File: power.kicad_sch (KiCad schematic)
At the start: 32 parts, among them J1 Barrel_Jack_MountingPin, J3 Conn_02x04_Odd_Even, Q1 SI2301CDS-T1-GE3, SW1 Power, U1 TPS54302

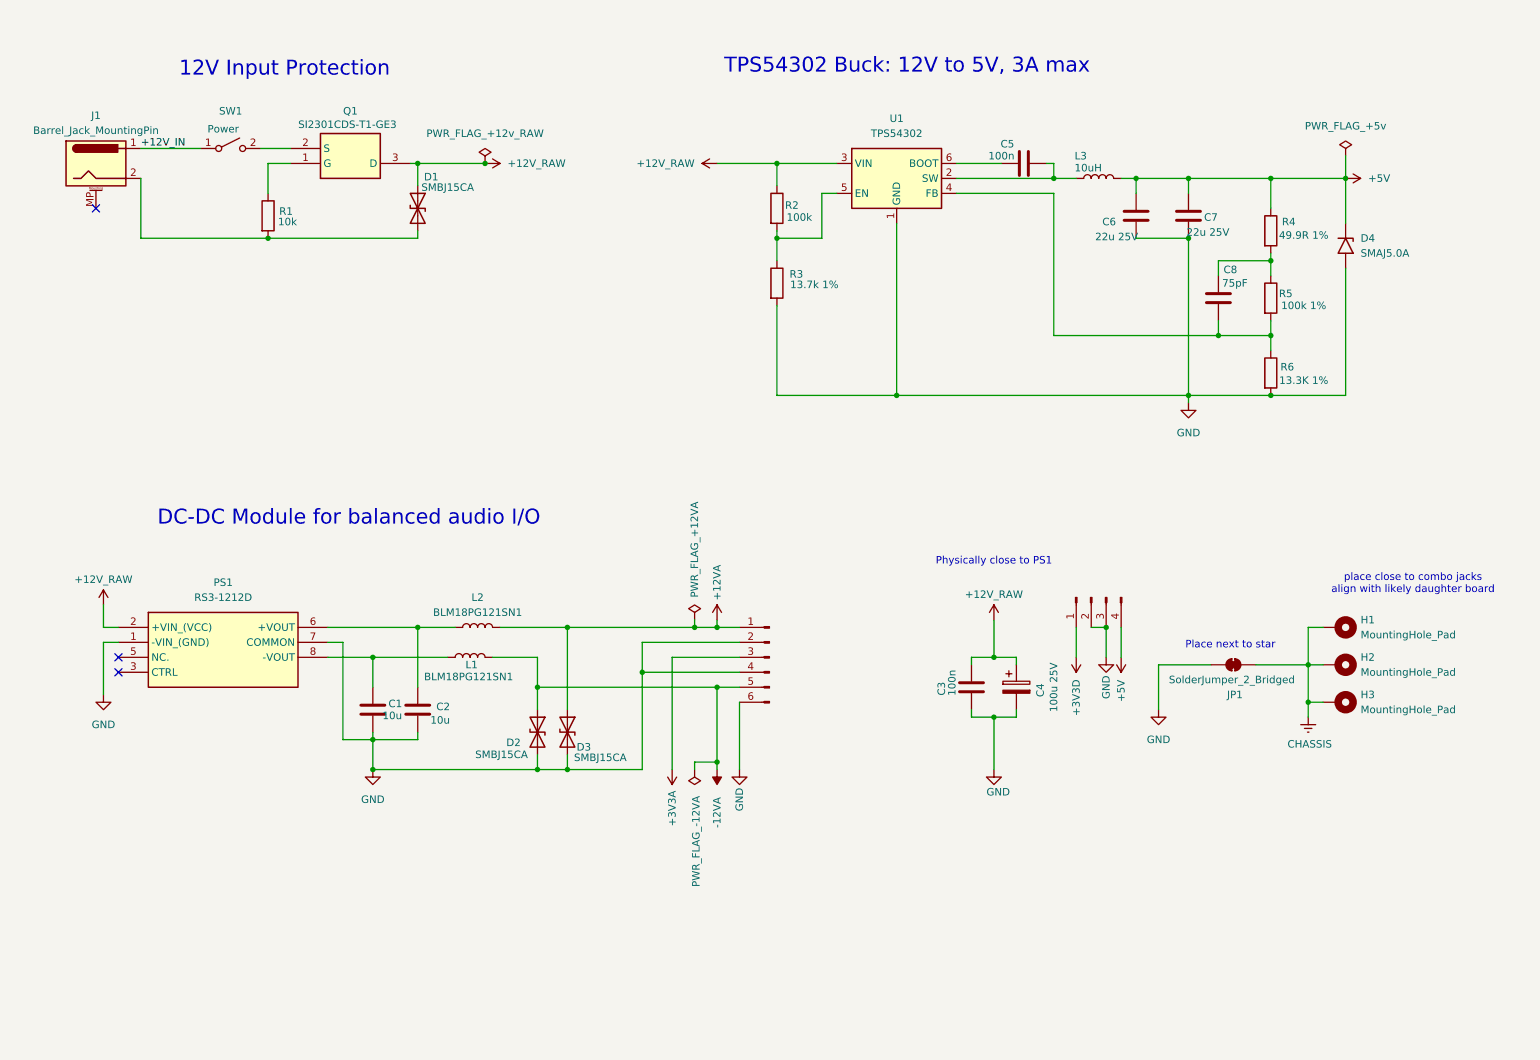
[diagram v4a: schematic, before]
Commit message: clean up some power cap issues
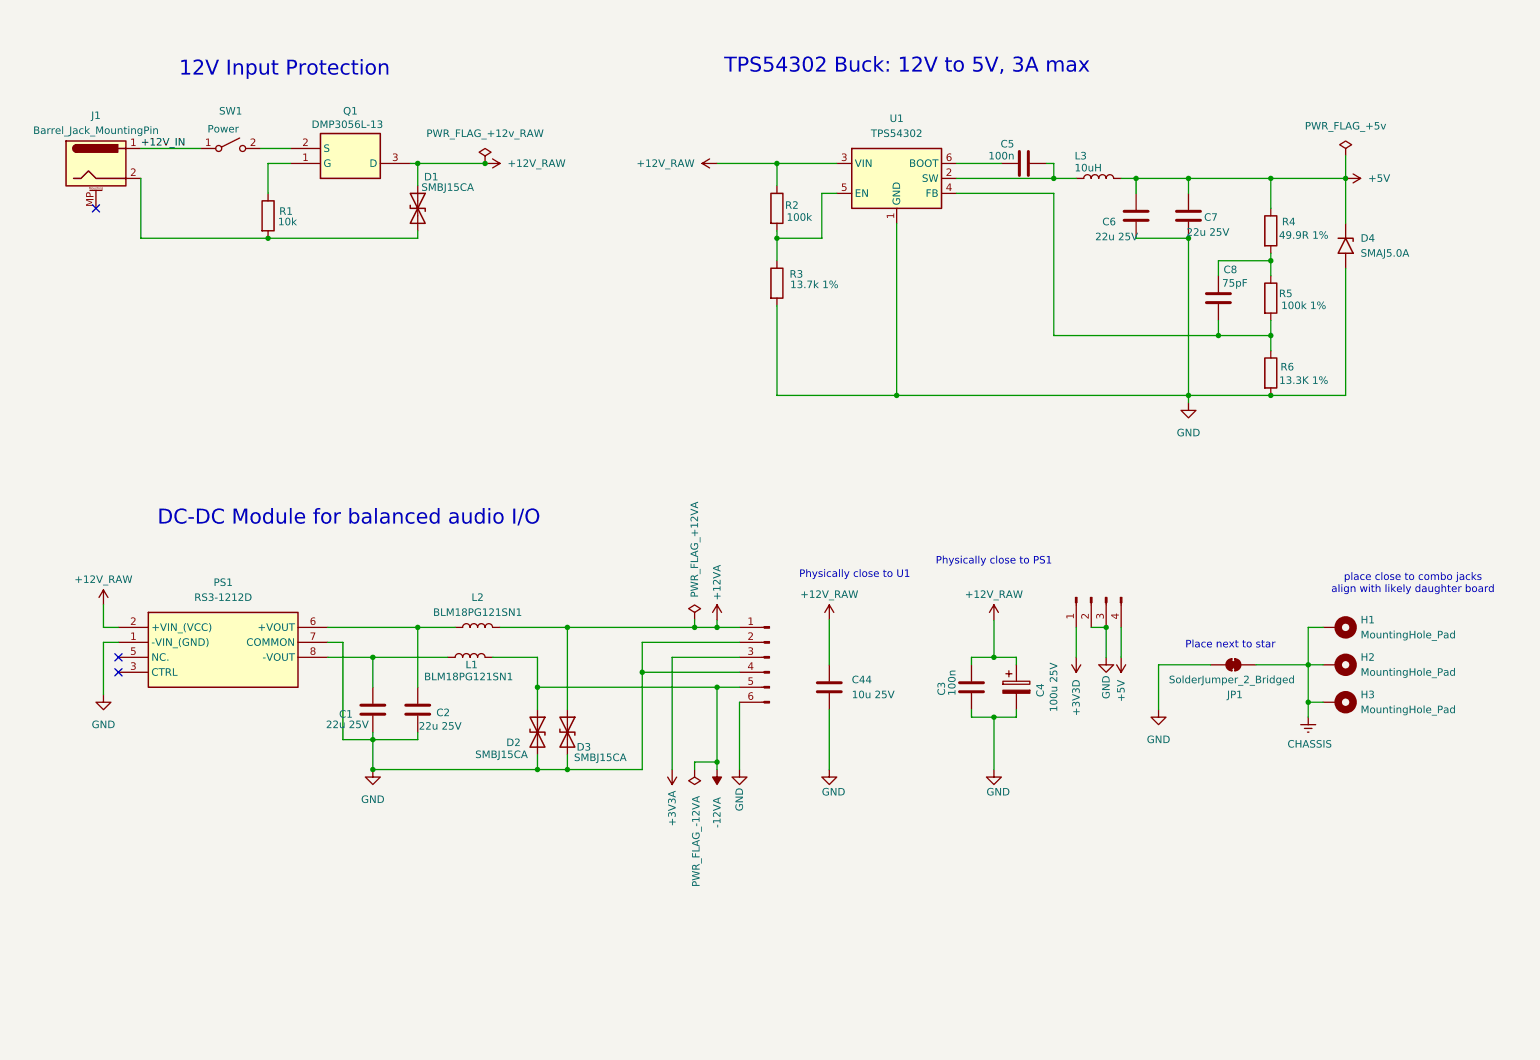
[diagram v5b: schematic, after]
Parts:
- added C44: 10u 25V, Capacitor_SMD:C_1206_3216Metric, symbol Device:C
- C1, C2: value 10u -> 22u 25V; footprint Capacitor_SMD:C_0805_2012Metric -> Capacitor_SMD:C_1206_3216Metric
- J3: value Conn_02x04_Odd_Even -> Conn_02x02_Odd_Even; footprint Connector_PinHeader_2.54mm:PinHeader_2x04_P2.54mm_Vertical -> Connector_PinHeader_2.54mm:PinHeader_2x02_P2.54mm_Vertical
- Q1: value SI2301CDS-T1-GE3 -> DMP3056L-13; footprint daisy-studio:SOT95P237X112-3N -> Package_TO_SOT_SMD:SOT-23-3; Manufacturer_Name Vishay -> Diodes Incorporated; Manufacturer_Part_Number SI2301CDS-T1-GE3 -> DMP3056L-13; Mouser Part Number 781-SI2301CDS-T1-GE3 -> 621-DMP3056L-13; Mouser Price/Stock https://www.mouser.co.uk/ProductDetail/Vishay-Semiconductor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 -> https://www.mouser.com/ProductDetail/Diodes-Incorporated/DM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
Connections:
- net +12V_RAW: now also C44.1
- net GND: now also C44.2
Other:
- note added: "Physically close to U1"

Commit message: final layout
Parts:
- renumbered C4 to C36, C5 to C37, C8 to C38, C44 to C39, C6 to C40, C7 to C41, C3 to C42, C2 to C43, C1 to C44, D3 to D12, D2 to D13, D1 to D14, D4 to D15, H2 to H4, H3 to H7, J3 to J12, J1 to J13, J2 to J8, L3 to L1, L1 to L3, Q1 to Q5, R1 to R33, R2 to R34, R5 to R35, R4 to R36, R3 to R37, R6 to R38, U1 to U10
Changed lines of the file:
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@@
 		(on_board yes)
 		(dnp no)
-		(property "Reference" "J2"
+		(property "Reference" "J8"
 			(at 139.192 141.224 90)
 			(effects
@@
 			(project "daisy-studio"
 				(path "/55cca6a8-30da-4c13-b2f2-a01401e2b54c/a1b2c3d4-1111-4000-8000-000000000001"
-					(reference "J2")
+					(reference "J8")
 					(unit 1)
 				)
@@
 		(on_board yes)
 		(dnp no)
-		(property "Reference" "C8"
+		(property "Reference" "C38"
 			(at 217.932 67.564 0)
 			(effects
@@
 			(project "triptech"
 				(path "/55cca6a8-30da-4c13-b2f2-a01401e2b54c/a1b2c3d4-1111-4000-8000-000000000001"
-					(reference "C8")
+					(reference "C38")
 					(unit 1)
 				)
@@
 		(on_board yes)
 		(dnp no)
-		(property "Reference" "J3"
+		(property "Reference" "J12"
 			(at 202.184 123.698 90)
 			(effects
@@
 			(project "daisy-studio"
 				(path "/55cca6a8-30da-4c13-b2f2-a01401e2b54c/a1b2c3d4-1111-4000-8000-000000000001"
-					(reference "J3")
+					(reference "J12")
 					(unit 1)
 				)
@@
 		(on_board yes)
 		(dnp no)
-		(property "Reference" "C1"
+		(property "Reference" "C44"
 			(at 67.818 143.002 0)
 			(effects
@@
 			(project "triptech"
 				(path "/55cca6a8-30da-4c13-b2f2-a01401e2b54c/a1b2c3d4-1111-4000-8000-000000000001"
-					(reference "C1")
+					(reference "C44")
 					(unit 1)
 				)
@@
 		(dnp no)
 		(fields_autoplaced yes)
-		(property "Reference" "C44"
+		(property "Reference" "C39"
 			(at 153.67 137.1599 0)
 			(effects
@@
 			(project ""
 				(path "/55cca6a8-30da-4c13-b2f2-a01401e2b54c/a1b2c3d4-1111-4000-8000-000000000001"
-					(reference "C44")
+					(reference "C39")
 					(unit 1)
 				)
@@
 		(on_board yes)
 		(dnp no)
-		(property "Reference" "R4"
+		(property "Reference" "R36"
 			(at 227.838 59.436 0)
 			(effects
@@
 			(project "triptech"
 				(path "/55cca6a8-30da-4c13-b2f2-a01401e2b54c/a1b2c3d4-1111-4000-8000-000000000001"
-					(reference "R4")
+					(reference "R36")
 					(unit 1)
 				)
@@
 		(on_board yes)
 		(dnp no)
-		(property "Reference" "C7"
+		(property "Reference" "C41"
 			(at 214.63 58.674 0)
 			(effects
@@
 			(project "triptech"
 				(path "/55cca6a8-30da-4c13-b2f2-a01401e2b54c/a1b2c3d4-1111-4000-8000-000000000001"
-					(reference "C7")
+					(reference "C41")
 					(unit 1)
 				)
@@
 		(on_board yes)
 		(dnp no)
-		(property "Reference" "D3"
+		(property "Reference" "D12"
 			(at 108.204 148.59 90)
 			(effects
@@
 			(project "daisy-studio"
 				(path "/55cca6a8-30da-4c13-b2f2-a01401e2b54c/a1b2c3d4-1111-4000-8000-000000000001"
-					(reference "D3")
+					(reference "D12")
 					(unit 1)
 				)
@@
 		(on_board yes)
 		(dnp no)
-		(property "Reference" "L1"
+		(property "Reference" "L3"
 			(at 89.154 134.62 90)
 			(effects
@@
 			(project "triptech"
 				(path "/55cca6a8-30da-4c13-b2f2-a01401e2b54c/a1b2c3d4-1111-4000-8000-000000000001"
-					(reference "L1")
+					(reference "L3")
 					(unit 1)
 				)
@@
 		(on_board yes)
 		(dnp no)
-		(property "Reference" "Q1"
+		(property "Reference" "Q5"
 			(at 68.58 40.64 0)
 			(effects
@@
 			(project "triptech"
 				(path "/55cca6a8-30da-4c13-b2f2-a01401e2b54c/a1b2c3d4-1111-4000-8000-000000000001"
-					(reference "Q1")
+					(reference "Q5")
 					(unit 1)
 				)
@@
 		(on_board yes)
 		(dnp no)
-		(property "Reference" "J1"
+		(property "Reference" "J13"
 			(at 25.4 41.402 0)
 			(effects
@@
 			(project "triptech"
 				(path "/55cca6a8-30da-4c13-b2f2-a01401e2b54c/a1b2c3d4-1111-4000-8000-000000000001"
-					(reference "J1")
+					(reference "J13")
 					(unit 1)
 				)
@@
 		(on_board yes)
 		(dnp no)
-		(property "Reference" "R1"
+		(property "Reference" "R33"
 			(at 57.658 57.658 0)
 			(effects
@@
 			(project "triptech"
 				(path "/55cca6a8-30da-4c13-b2f2-a01401e2b54c/a1b2c3d4-1111-4000-8000-000000000001"
-					(reference "R1")
+					(reference "R33")
 					(unit 1)
 				)
@@
 		(on_board yes)
 		(dnp no)
-		(property "Reference" "D1"
+		(property "Reference" "D14"
 			(at 82.296 51.816 90)
 			(effects
@@
 			(project "triptech"
 				(path "/55cca6a8-30da-4c13-b2f2-a01401e2b54c/a1b2c3d4-1111-4000-8000-000000000001"
-					(reference "D1")
+					(reference "D14")
 					(unit 1)
 				)
@@
 		(on_board yes)
 		(dnp no)
-		(property "Reference" "C4"
+		(property "Reference" "C36"
 			(at 185.674 138.938 90)
 			(effects
@@
 			(project "triptech"
 				(path "/55cca6a8-30da-4c13-b2f2-a01401e2b54c/a1b2c3d4-1111-4000-8000-000000000001"
-					(reference "C4")
+					(reference "C36")
 					(unit 1)
 				)
@@
 		(on_board yes)
 		(dnp no)
-		(property "Reference" "C3"
+		(property "Reference" "C42"
 			(at 168.91 138.684 90)
 			(effects
@@
 			(project "triptech"
 				(path "/55cca6a8-30da-4c13-b2f2-a01401e2b54c/a1b2c3d4-1111-4000-8000-000000000001"
-					(reference "C3")
+					(reference "C42")
 					(unit 1)
 				)
@@
 		(on_board yes)
 		(dnp no)
-		(property "Reference" "C5"
+		(property "Reference" "C37"
 			(at 180.086 46.228 90)
 			(effects
@@
 			(project "triptech"
 				(path "/55cca6a8-30da-4c13-b2f2-a01401e2b54c/a1b2c3d4-1111-4000-8000-000000000001"
-					(reference "C5")
+					(reference "C37")
 					(unit 1)
 				)
@@
 		(on_board yes)
 		(dnp no)
-		(property "Reference" "L3"
+		(property "Reference" "L1"
 			(at 192.532 48.26 90)
 			(effects
@@
 			(project "triptech"
 				(path "/55cca6a8-30da-4c13-b2f2-a01401e2b54c/a1b2c3d4-1111-4000-8000-000000000001"
-					(reference "L3")
+					(reference "L1")
 					(unit 1)
 				)
@@
 		(on_board yes)
 		(dnp no)
-		(property "Reference" "R2"
+		(property "Reference" "R34"
 			(at 143.51 56.642 0)
 			(effects
@@
 			(project "triptech"
 				(path "/55cca6a8-30da-4c13-b2f2-a01401e2b54c/a1b2c3d4-1111-4000-8000-000000000001"
-					(reference "R2")
+					(reference "R34")
 					(unit 1)
 				)
@@
 		(on_board yes)
 		(dnp no)
-		(property "Reference" "R3"
+		(property "Reference" "R37"
 			(at 144.272 68.326 0)
 			(effects
@@
 			(project "triptech"
 				(path "/55cca6a8-30da-4c13-b2f2-a01401e2b54c/a1b2c3d4-1111-4000-8000-000000000001"
-					(reference "R3")
+					(reference "R37")
 					(unit 1)
 				)
@@
 		(on_board yes)
 		(dnp no)
-		(property "Reference" "R5"
+		(property "Reference" "R35"
 			(at 227.33 71.628 0)
 			(effects
@@
 			(project "triptech"
 				(path "/55cca6a8-30da-4c13-b2f2-a01401e2b54c/a1b2c3d4-1111-4000-8000-000000000001"
-					(reference "R5")
+					(reference "R35")
 					(unit 1)
 				)
@@
 		(on_board yes)
 		(dnp no)
-		(property "Reference" "R6"
+		(property "Reference" "R38"
 			(at 227.584 84.074 0)
 			(effects
@@
 			(project "triptech"
 				(path "/55cca6a8-30da-4c13-b2f2-a01401e2b54c/a1b2c3d4-1111-4000-8000-000000000001"
-					(reference "R6")
+					(reference "R38")
 					(unit 1)
 				)
@@
 		(on_board yes)
 		(dnp no)
-		(property "Reference" "C6"
+		(property "Reference" "C40"
 			(at 197.358 59.436 0)
 			(effects
@@
 			(project "triptech"
 				(path "/55cca6a8-30da-4c13-b2f2-a01401e2b54c/a1b2c3d4-1111-4000-8000-000000000001"
-					(reference "C6")
+					(reference "C40")
 					(unit 1)
 				)
@@
 		(on_board yes)
 		(dnp no)
-		(property "Reference" "C2"
+		(property "Reference" "C43"
 			(at 84.328 142.748 0)
 			(effects
@@
 			(project "triptech"
 				(path "/55cca6a8-30da-4c13-b2f2-a01401e2b54c/a1b2c3d4-1111-4000-8000-000000000001"
-					(reference "C2")
+					(reference "C43")
 					(unit 1)
 				)
@@
 		(dnp no)
 		(fields_autoplaced yes)
-		(property "Reference" "U1"
+		(property "Reference" "U10"
 			(at 161.29 41.91 0)
 			(effects
@@
 			(project "triptech"
 				(path "/55cca6a8-30da-4c13-b2f2-a01401e2b54c/a1b2c3d4-1111-4000-8000-000000000001"
-					(reference "U1")
+					(reference "U10")
 					(unit 1)
 				)
@@
 		(on_board yes)
 		(dnp no)
-		(property "Reference" "D2"
+		(property "Reference" "D13"
 			(at 96.266 147.828 90)
 			(effects
@@
 			(project "daisy-studio"
 				(path "/55cca6a8-30da-4c13-b2f2-a01401e2b54c/a1b2c3d4-1111-4000-8000-000000000001"
-					(reference "D2")
+					(reference "D13")
 					(unit 1)
 				)
@@
 		(dnp no)
 		(fields_autoplaced yes)
-		(property "Reference" "H3"
+		(property "Reference" "H7"
 			(at 240.03 139.6999 90)
 			(effects
@@
 			(project "daisy-studio"
 				(path "/55cca6a8-30da-4c13-b2f2-a01401e2b54c/a1b2c3d4-1111-4000-8000-000000000001"
-					(reference "H3")
+					(reference "H7")
 					(unit 1)
 				)
@@
 		(dnp no)
 		(fields_autoplaced yes)
-		(property "Reference" "D4"
+		(property "Reference" "D15"
 			(at 240.03 62.2299 90)
 			(effects
@@
 			(project ""
 				(path "/55cca6a8-30da-4c13-b2f2-a01401e2b54c/a1b2c3d4-1111-4000-8000-000000000001"
-					(reference "D4")
+					(reference "D15")
 					(unit 1)
 				)
@@
 		(dnp no)
 		(fields_autoplaced yes)
-		(property "Reference" "H2"
+		(property "Reference" "H4"
 			(at 240.03 133.3499 90)
 			(effects
@@
 			(project "daisy-studio"
 				(path "/55cca6a8-30da-4c13-b2f2-a01401e2b54c/a1b2c3d4-1111-4000-8000-000000000001"
-					(reference "H2")
+					(reference "H4")
 					(unit 1)
 				)
